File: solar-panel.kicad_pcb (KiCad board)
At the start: 2 copper layers, 327.5 x 87 mm, 36 parts, among them J101 Conn_01x05_Pin, J102 Conn_01x02, U101 MCP3008, U201 SS39ET, U301 LMT87DCK, U401 LMT87DCK

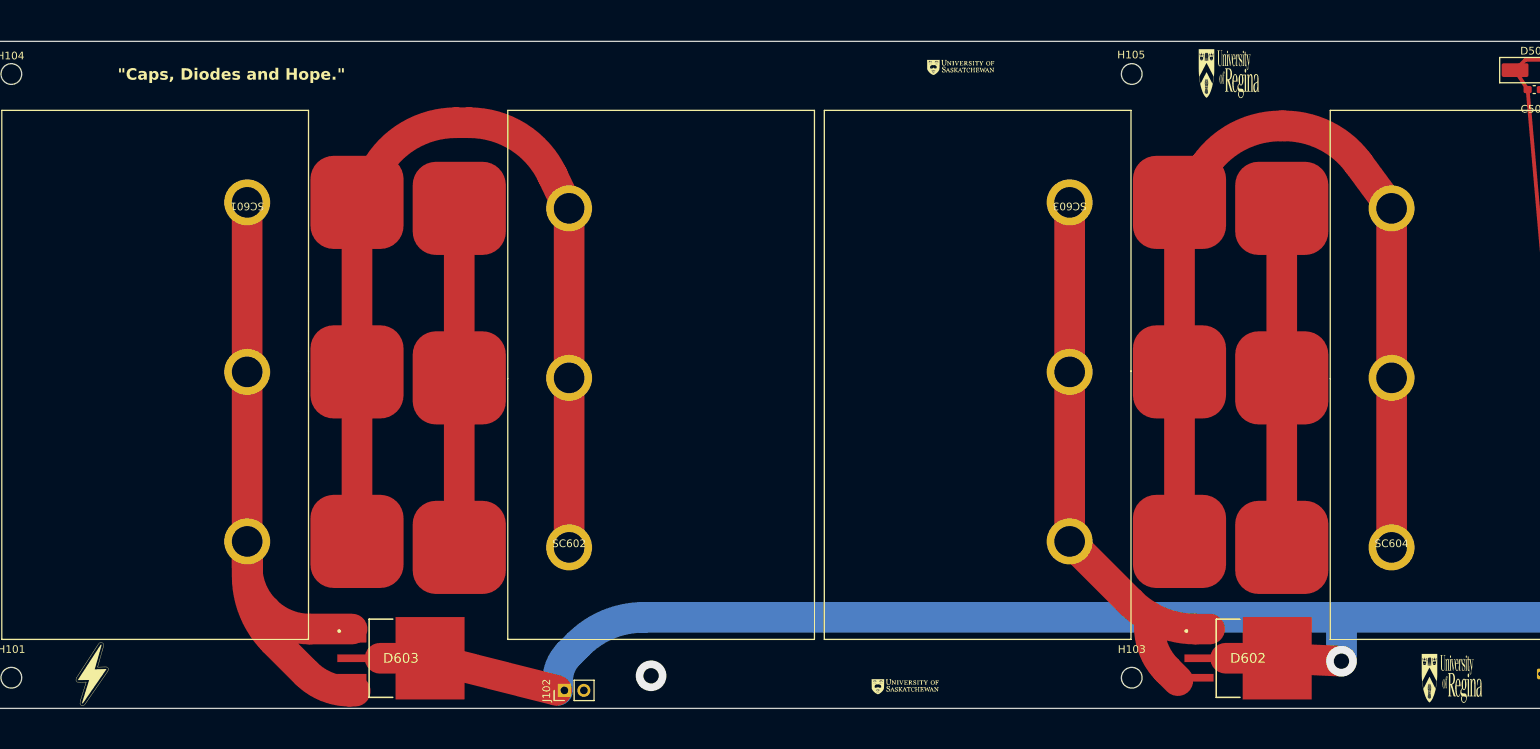
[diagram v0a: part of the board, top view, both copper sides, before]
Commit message: added silkscreen
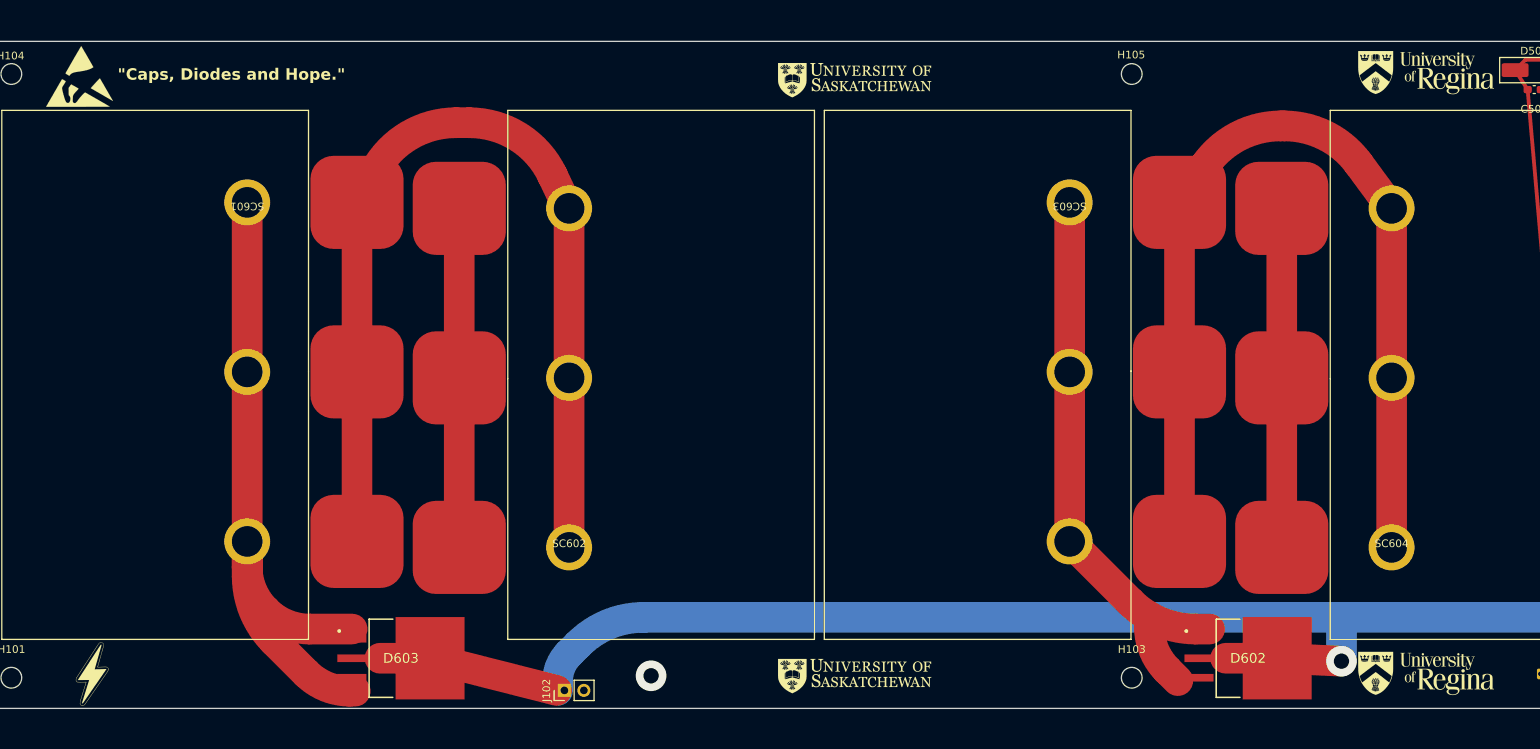
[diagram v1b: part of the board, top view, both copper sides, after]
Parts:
- removed the G*** at (236.0, 185.2)
- removed the G*** at (206.9, 106.3)
- removed the G*** at (164.7, 186.3)
- removed the G*** at (172.0, 105.5)
- added G***: LOGO, USST_logo:u_of_r_logo_20x8, F.Cu at (232.5, 106.2)
- added G***: LOGO, USST_logo:usask_logo_20x4, F.Cu at (158.1, 184.9)
- added G***: LOGO, USST_logo:u_of_r_logo_20x8, F.Cu at (232.5, 184.5)
- added G***: LOGO, USST_logo:usask_logo_20x4, F.Cu at (158.1, 107.2)
- added REF**: ESD-Logo_8.9x8mm_SilkScreen, Symbol:ESD-Logo_8.9x8mm_SilkScreen, F.Cu at (57.0, 106.7)

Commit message: not done yet
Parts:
- removed the G*** at (232.5, 106.2)
- removed the G*** at (158.1, 107.2)
- REF**: moved to B.Cu
- moved J102 12.2 mm to (118.0, 174.8)
- moved H106 10.3 mm to (377.2, 106.8)
- moved H102 8.47 mm to (358.5, 184.1)
- moved C201 7.73 mm to (265.5, 109.2), turned to -90 degrees
- moved REF** 6.93 mm to (52.9, 112.3), turned to 180 degrees
- moved D601 5.39 mm to (309.4, 182.6)
- moved G*** 5.39 mm to (152.7, 184.9)
- moved J101 5.39 mm to (242.2, 184.6)
- moved G*** 5.39 mm to (53.3, 184.7)
- moved H104 5.39 mm to (42.7, 106.4)
- moved C101 5.39 mm to (263.5, 186.9)
- moved C401 5.39 mm to (270.3, 185.6)
- moved G*** 5.39 mm to (345.9, 184.7)
- moved H103 5.39 mm to (188.9, 185.1)
- moved H105 5.39 mm to (188.9, 106.4)
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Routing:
- net /Sun sensor/PHOTO_OUT: track 86.0 -> 78.7 mm
- net +3.3V: track 137.0 -> 131.1 mm
- net Net-(SC605--): track 130.7 -> 127.2 mm
- net GND: track 136.7 -> 133.6 mm
- net /Temp Sensor 2/TEMP_OUT: track 73.7 -> 71.7 mm
- net /Solar Cells/PV_V+: track 242.9 -> 241.2 mm, vias 2 -> 3
- net /Mag Sensor/MAG_OUT: track 72.6 -> 71.9 mm
- net (no net): vias 2 -> 0
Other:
- board size 327.5 x 87 mm -> 320 x 82 mm

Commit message: 1st change - moved mounting holes
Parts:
- moved H106 59.9 mm to (317.5, 111.8)
- moved H104 46.5 mm to (88.9, 111.8)
- moved H105 8.60 mm to (195.6, 111.8)
- moved H101 2.65 mm to (50.8, 185.4)
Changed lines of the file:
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@@
   )
   (footprint "MountingHole:MountingHole_2.7mm" (layer "F.Cu")
-    (at 48.4796 184.13)
+    (at 50.8 185.42)
     (descr "Mounting Hole 2.7mm, no annular")
     (tags "mounting hole 2.7mm no annular")
@@
   )
   (footprint "MountingHole:MountingHole_2.7mm" (layer "F.Cu")
-    (at 377.22 106.84)
+    (at 317.5 111.76)
     (descr "Mounting Hole 2.7mm, no annular")
     (tags "mounting hole 2.7mm no annular")
@@
   )
   (footprint "MountingHole:MountingHole_2.7mm" (layer "F.Cu")
-    (at 188.859 106.389)
+    (at 195.58 111.76)
     (descr "Mounting Hole 2.7mm, no annular")
     (tags "mounting hole 2.7mm no annular")
@@
   )
   (footprint "MountingHole:MountingHole_2.7mm" (layer "F.Cu")
-    (at 42.729 106.389)
+    (at 88.9 111.76)
     (descr "Mounting Hole 2.7mm, no annular")
     (tags "mounting hole 2.7mm no annular")

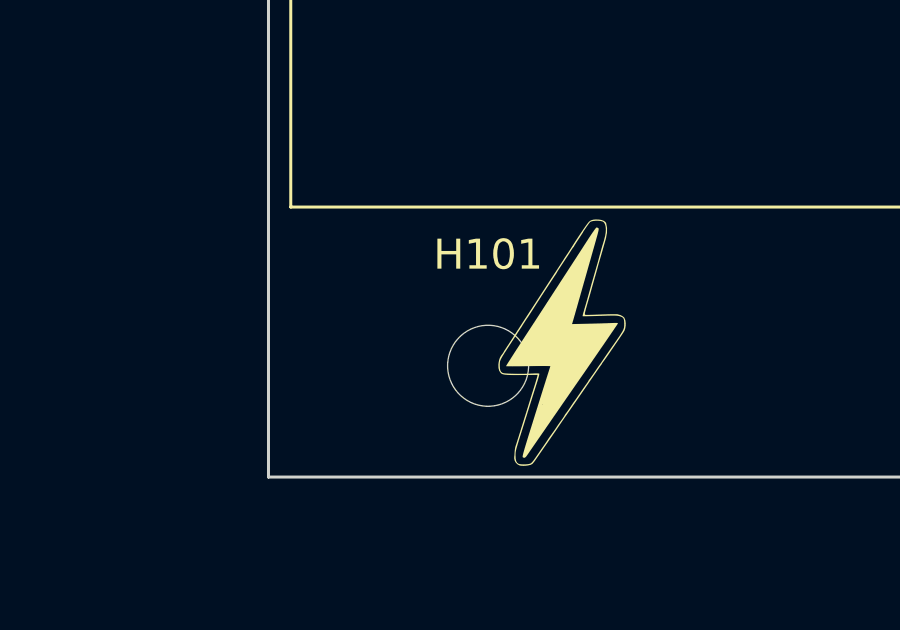
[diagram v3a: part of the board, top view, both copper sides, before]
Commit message: 1st draft - moved mounting holes
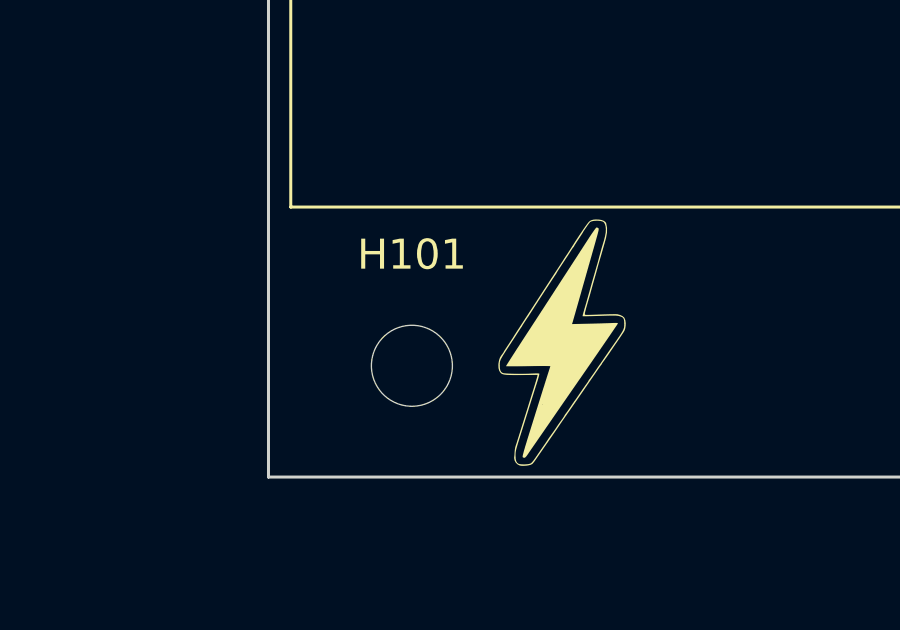
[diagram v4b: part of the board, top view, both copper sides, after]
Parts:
- moved H101 2.54 mm to (48.3, 185.4)
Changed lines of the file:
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@@
   )
   (footprint "MountingHole:MountingHole_2.7mm" (layer "F.Cu")
-    (at 50.8 185.42)
+    (at 48.26 185.42)
     (descr "Mounting Hole 2.7mm, no annular")
     (tags "mounting hole 2.7mm no annular")

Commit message: new branch
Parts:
- J101: moved to F.Cu
- moved H106 40.9 mm to (358.4, 110.5)
- moved H104 40.8 mm to (48.2, 110.3)
- moved SC605 2.56 mm to (330.7, 170.7)
- moved SC601 2.50 mm to (77.1, 125.5)
- moved H102 1.80 mm to (358.4, 185.9)
- moved H101 0.45 mm to (48.1, 185.8)
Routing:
- net Net-(D601-ANODE_1): track 94.8 -> 85.8 mm
- net Net-(D603-ANODE_1): track 92.6 -> 84.9 mm
